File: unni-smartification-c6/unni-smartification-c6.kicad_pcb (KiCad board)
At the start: 4 copper layers, 83.3 x 65 mm, 75 parts, among them J1 UJ20-C-H-G-SMT-1-P16-TR, J10 B6B-PH-K-S, J2 B2B-PH-K-S, J3 B6B-PH-K-S, J4 S3B-PH-SM4-TB, J5 B3B-PH-K-S, J6 B5B-PH-K-S, Q1 AO3401A, Q10 AO3400A, Q2 AO3401A, Q3 AO3400A, Q4 AO3400A, SW1 RESET, SW2 BOOT, U1 MCP73831, U10 ESP32-C6-MINI-1-N4, U2 TPS63031, U3 TPS613222A, U4 TPD2E009DBZR

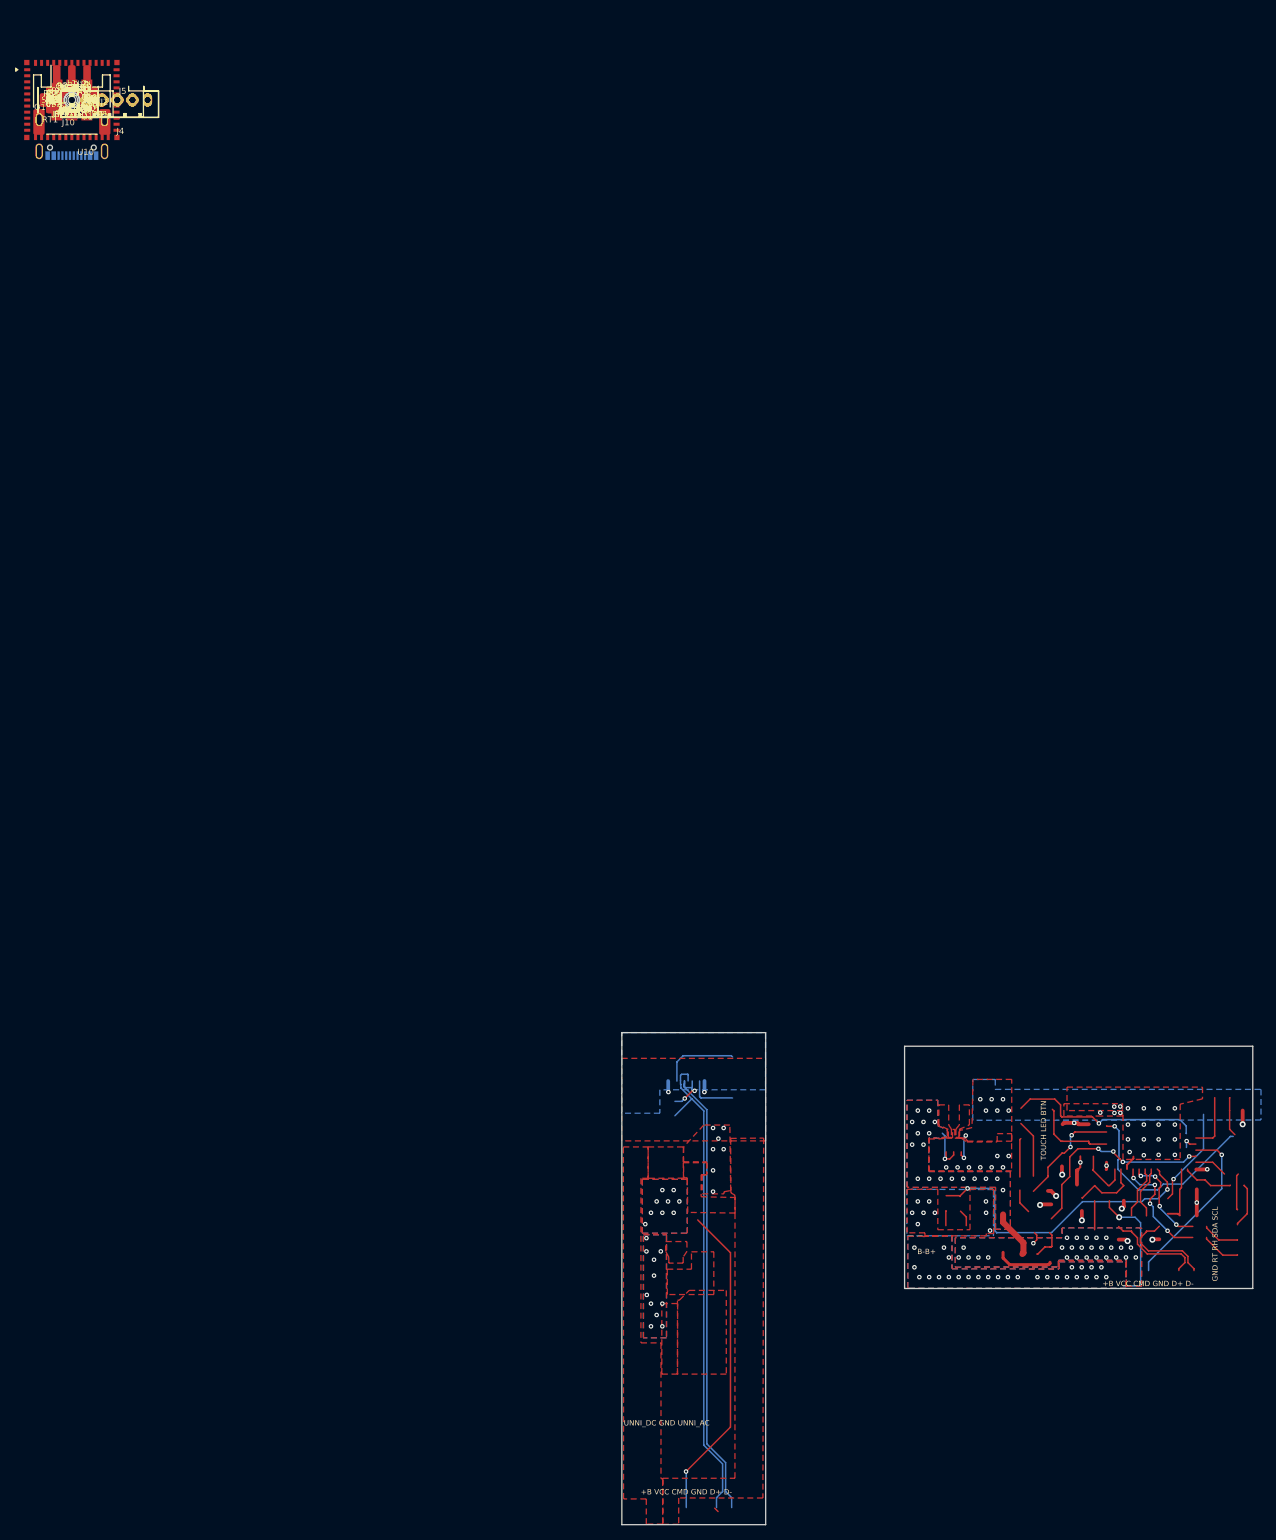
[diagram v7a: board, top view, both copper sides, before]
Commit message: update PCB layout a bit
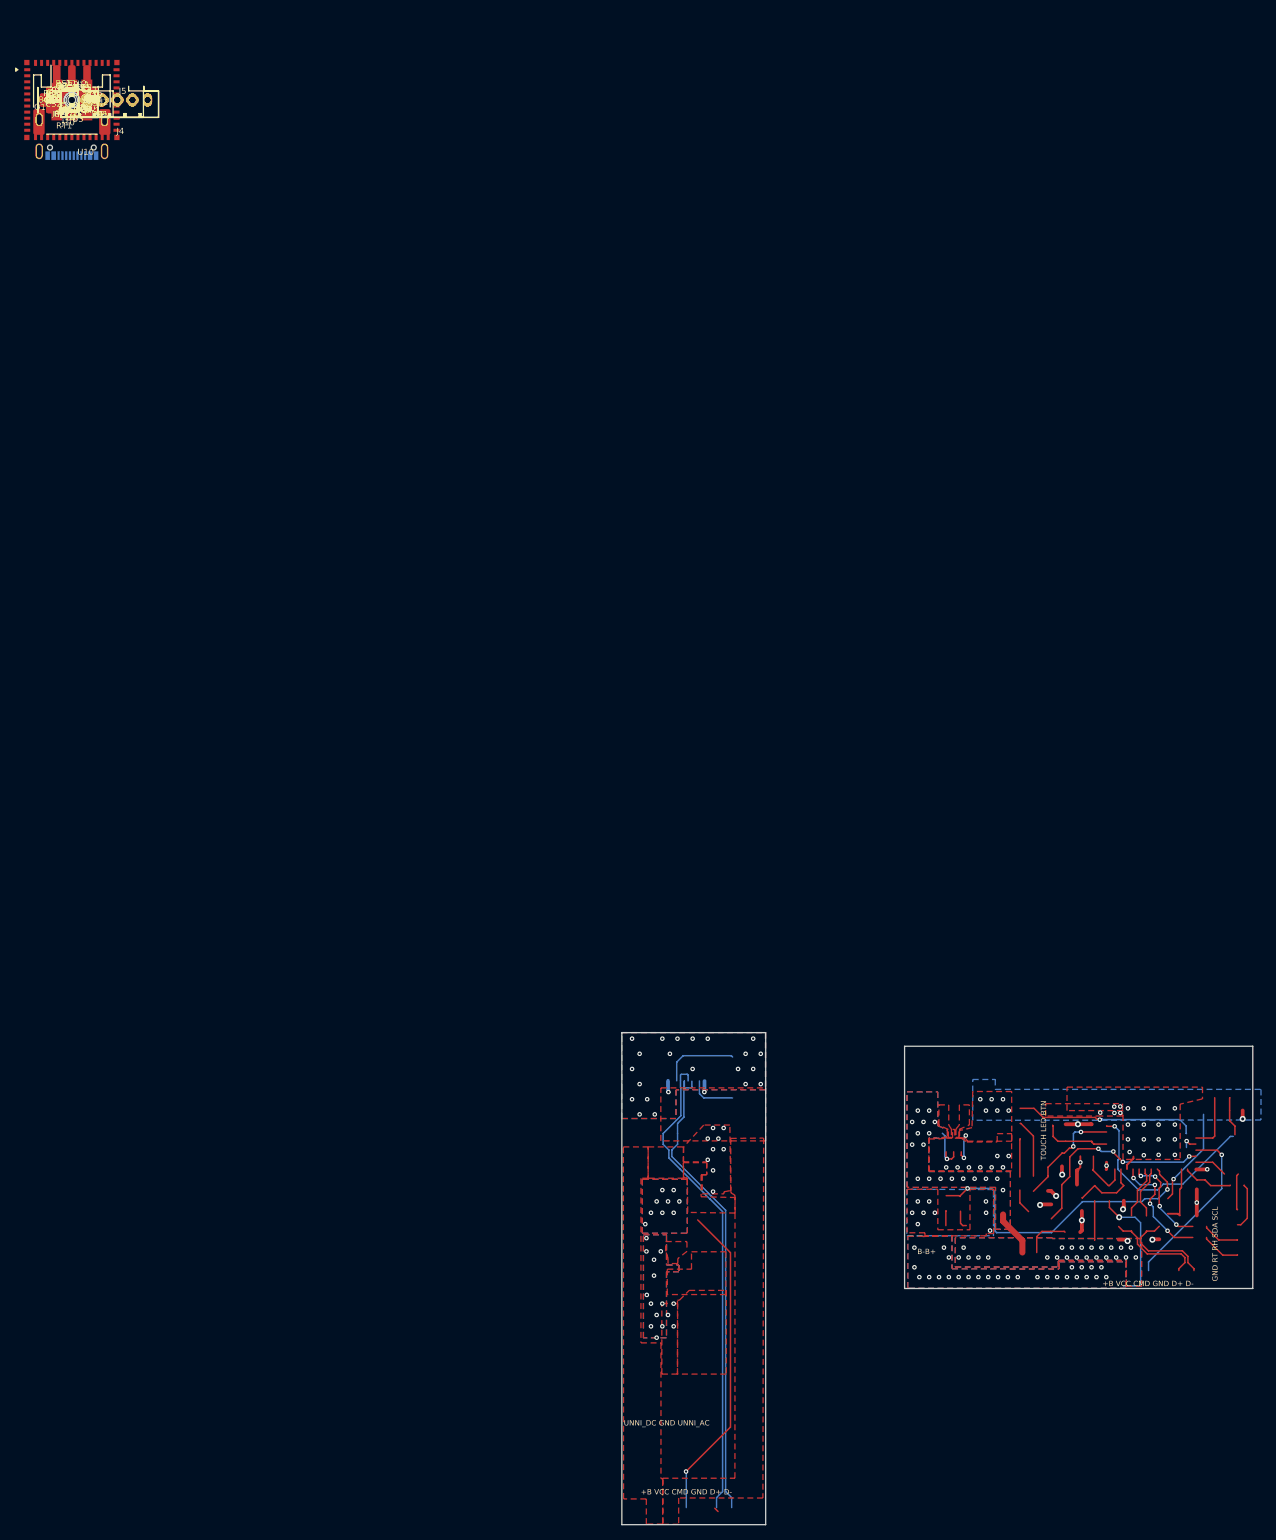
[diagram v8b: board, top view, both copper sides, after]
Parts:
- SW1: value RESET -> RST
- U3: value TPS613222A -> TPS613222ADBV; footprint Package_TO_SOT_SMD:SOT-23_Handsoldering -> Package_TO_SOT_SMD:SOT-23-5
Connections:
- U3 pad 1: +5V -> Net-(U3-SW)
- U3 pad 2: Net-(U3-SW) -> GND
- U3 pad 3: GND -> unconnected-(U3-NC-Pad3)
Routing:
- net VBUS: track 14.3 -> 8.12 mm, vias 28 -> 25
- net USB_RAW_P: track 78.6 -> 76.0 mm, vias 2 -> 0
- net CONN_BTN: track 26.1 -> 24.0 mm
- net /ESP32-C6 + Auxiliary/ESP_EN: track 11.0 -> 9.05 mm
- net Net-(Q1-G): track 4.37 -> 6.17 mm
- net USB_RAW_N: track 78.5 -> 77.2 mm
- net GND: track 27.5 -> 26.6 mm, vias 65 -> 91
